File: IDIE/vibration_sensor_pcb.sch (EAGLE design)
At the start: 37 parts, among them IC1 LORA-E5, IC2 STM32L071KBT6, IC3 FXLS8974CFR3, IC4 FXLS8971CFR1, IC5 DRV5032FBLPGM5HZ, Q2 SI2305B-TP, Y1 ABS06-32.768KHZ-9-1-T

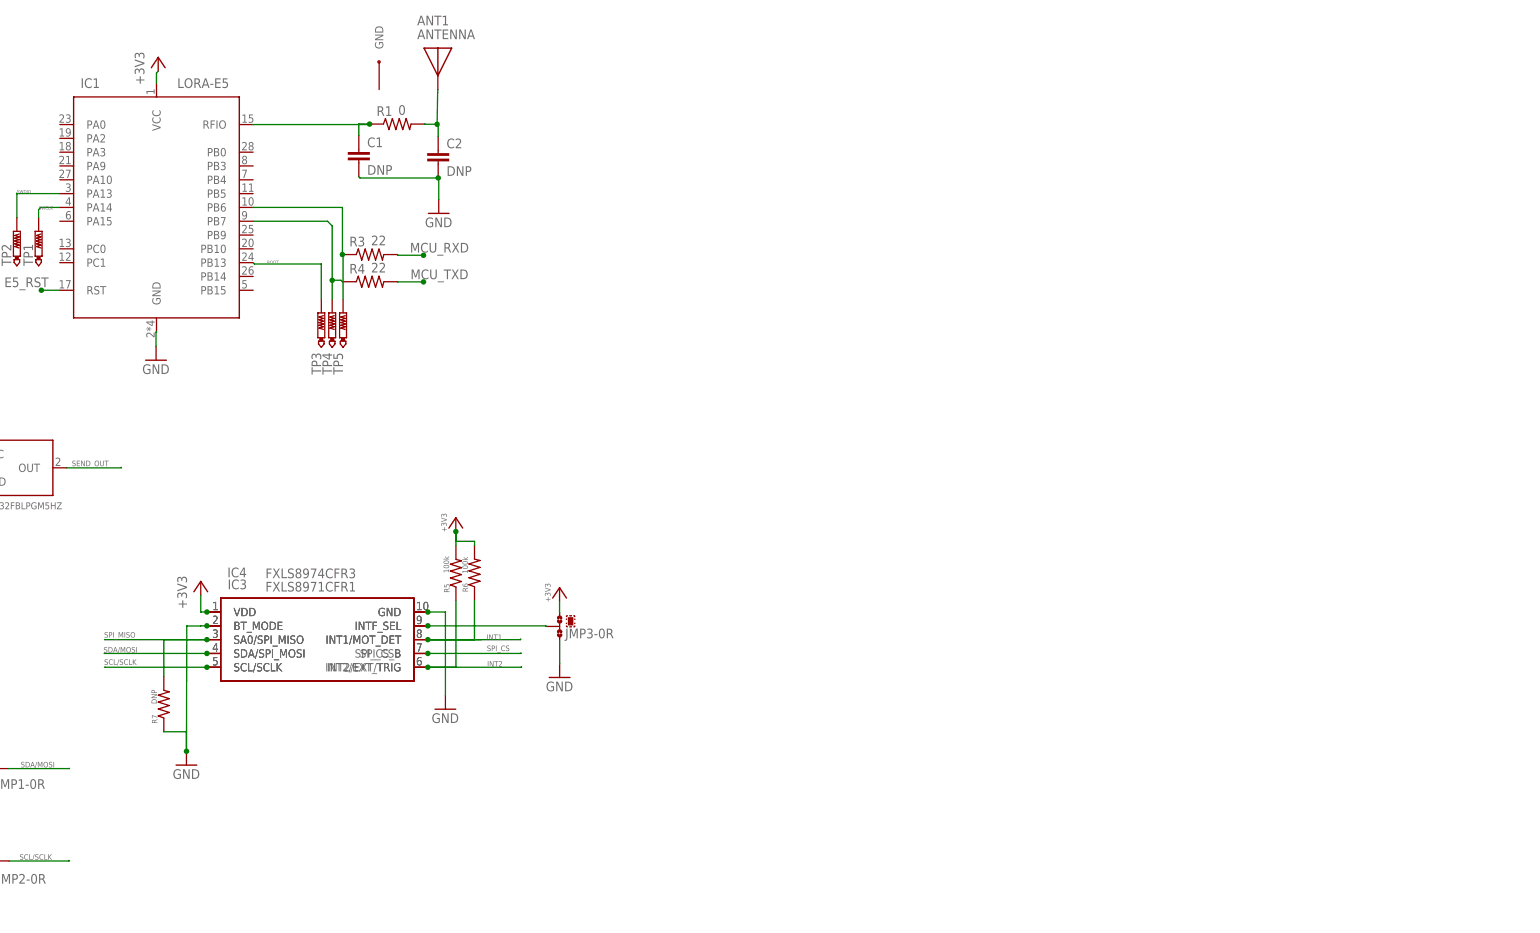
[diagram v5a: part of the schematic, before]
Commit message: UPDATE nueva hoja con usb y diversas conecciones antes de ruteo
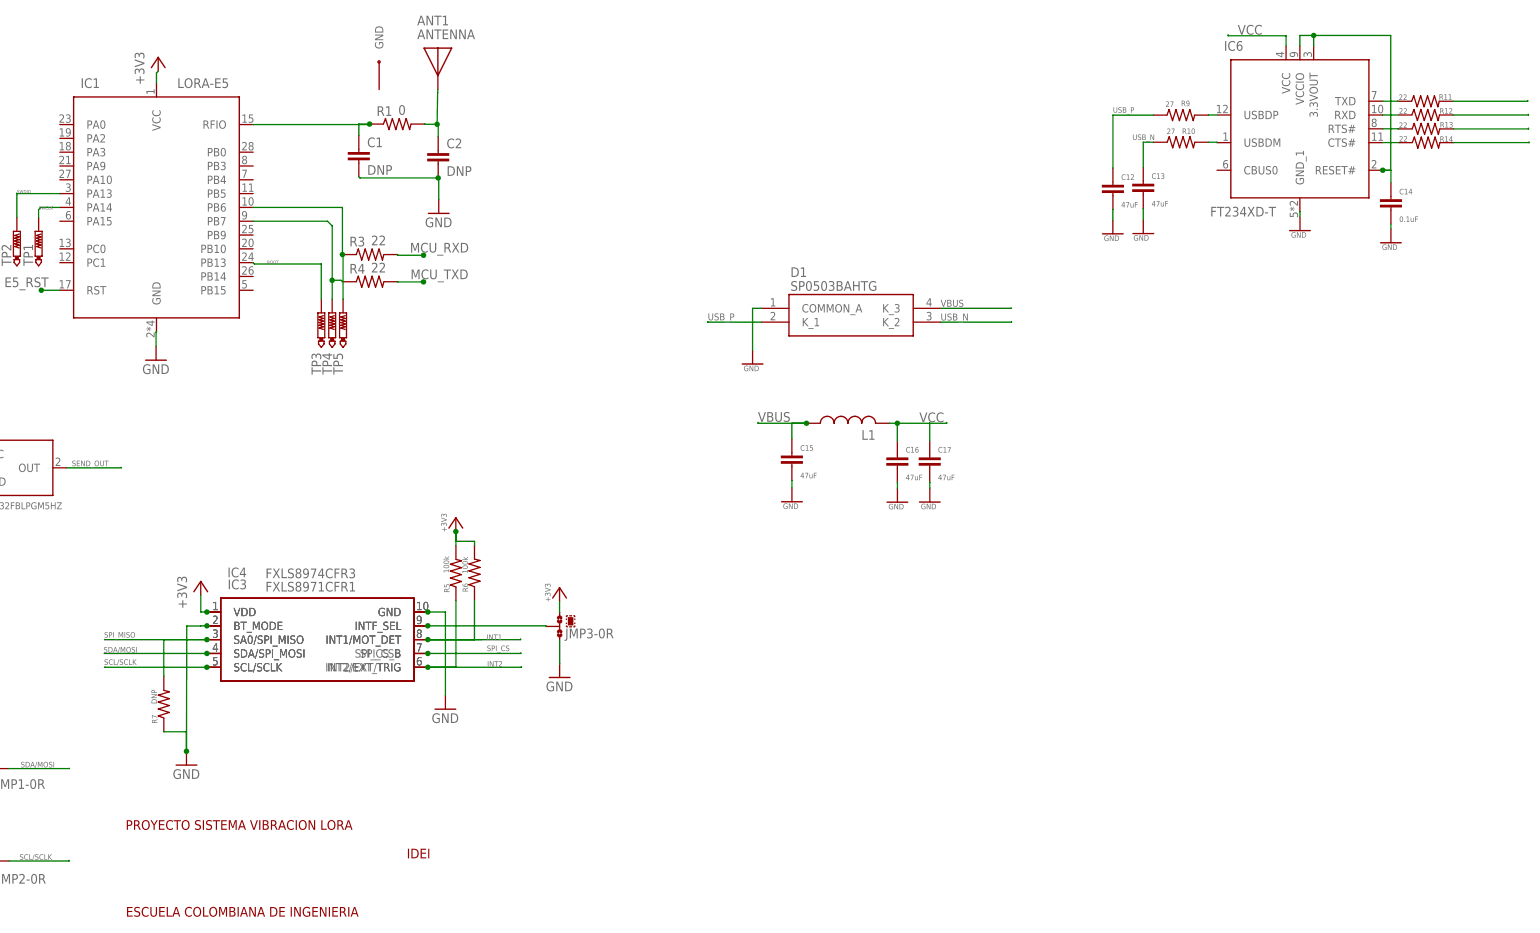
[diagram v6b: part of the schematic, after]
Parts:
- added C12, C13, C15, C16, C17: 47uF, rcl:C-EUC0603
- added C14: 0.1uF, rcl:C-EUC0603
- added D1: SP0503BAHTG, SamacSys_Parts:SP0503BAHTG
- added IC6: FT234XD-T, SamacSys_Parts:FT234XD-T
- added L1: (no value), rcl:L-US
- added R10, R9: 27, rcl:R-US_R0603
- added R11, R12, R13, R14: 22, rcl:R-US_R0603
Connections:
- new net N$10: IC6.USBDP, R9.2
- new net N$11: IC6.USBDM, R10.2
- new net N$12: IC6.TXD, R11.1
- new net N$13: IC6.RXD, R12.1
- new net N$14: IC6.RTS#, R13.1
- new net N$16: IC6.CTS#, R14.1
- new net N$17: R11.2
- new net N$18: R12.2
- new net N$19: R13.2
- new net N$20: R14.2
- new net N$9: C14.1, IC6.3.3VOUT, IC6.RESET#, IC6.VCCIO
- new net USB_N: C13.1, D1.K_2, R10.1
- new net USB_P: C12.1, D1.K_1, R9.1
- new net VBUS: C15.1, D1.K_3, L1.1
- new net VCC: C16.1, C17.1, IC6.VCC, L1.2
- net GND: now also C12.2, C13.2, C14.2, C15.2, C16.2, C17.2, D1.COMMON_A, IC6.GND_1
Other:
- note added: "ESCUELA COLOMBIANA DE INGENIERIA"
- note added: "IDEI"
- note added: "PROYECTO SISTEMA VIBRACION LORA"

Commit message: UPDATE casi terminacion del diseño, cambiar efecto hall y conectar ruteo
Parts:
- added C18: CLY6D-FKC-CK1N1D1BB7D3D3, SamacSys_Parts:CLY6D-FKC-CK1N1D1BB7D3D3
- added J1: 217182-0001, SamacSys_Parts:217182-0001
- added R15, R16: 27, rcl:R-US_R0603
- added R17, R18, R19: 22, rcl:R-US_R0603
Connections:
- removed net N$17: R11.2
- removed net N$18: R12.2
- removed net N$19: R13.2
- removed net N$20: R14.2
- removed net PA8: IC2.PA8
- removed net PB3: IC2.PB3
- removed net PB4: IC2.PB4
- removed net PB6: IC2.PB6
- removed net PB7: IC2.PB7
- new net LED_B: IC2.PB0, R17.2
- new net LED_G: IC2.PB1, R18.2
- new net LED_R: IC2.PA8, R19.2
- new net N$15: C18.A-BLUE, R17.1
- new net N$21: J1.B5, R15.2
- new net N$22: J1.A5, R16.2
- new net N$23: C18.A-GREEN, R18.1
- new net N$24: C18.A-RED, R19.1
- new net PA0: IC2.PA0
- new net PA11: IC2.PA11
- new net PA12: IC2.PA12
- new net U1_CTS: IC2.PB4, R13.2
- new net U1_RTS: IC2.PB3, R14.2
- new net U1_RXD: IC2.PB7, R11.2
- new net U1_TXD: IC2.PB6, R12.2
- net GND: now also C18.K-BLUE, C18.K-GREEN, C18.K-RED, J1.A1, J1.A12, J1.B1, J1.B12, J1.MH2, J1.MH3, J1.MH5, J1.MH6, R15.1, R16.1
- net SEND_OUT: now also IC2.PA1
- net USB_N: now also J1.A7, J1.B7
- net USB_P: now also J1.A6, J1.B6
- net VBUS: now also J1.A4, J1.A9, J1.B4, J1.B9
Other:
- note added: "cambiar por smd"
- moved on the sheet: C12, C13, C14, C15, C16, C17, D1, IC6, L1, R10, R11, R12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

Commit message: UPDATE orden de pcb y reglas de diseño
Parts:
- added FD1, FD2, FD3, FD4: TPTP10R, testpad:TPTP10R
- IC5: value DRV5032FBLPGM5HZ -> DRV5032FBLPGM; device transistor:DRV5032FBLPGM5HZ -> transistor:DRV5032FBLPGM
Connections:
- net N$10 renamed USBDP
- net N$11 renamed USBDM
- net N$12 renamed R11
- net N$13 renamed R12
- net N$14 renamed R13
- net N$15 renamed R17
- net N$16 renamed R14
- net N$2 renamed IN_MOSFET
- net N$21 renamed B5
- net N$22 renamed A5
- net N$23 renamed R18
- net N$24 renamed R19
- net N$3 renamed LORA_RXD
- net N$4 renamed LORA_TXD
- net N$7 renamed OSC32_IN
- net N$8 renamed OSC32_OUT
- net RF_IO renamed OUT_ANT
- removed net SPI_SCK: IC2.PA5
- net SPI_SCLK: now also IC2.PA5
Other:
- note removed: "cambiar por smd"
- moved on the sheet: C15, C16, C17, C18, C5, IC3, IC4, IC5, JMP1-0R, JMP2-0R, JMP3-0R, L1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
